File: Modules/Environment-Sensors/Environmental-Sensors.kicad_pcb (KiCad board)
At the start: 2 copper layers, 20.3 x 18.4 mm, 15 parts, among them J1 Conn_01x04, U1 CCS811, U2 ENS210, U3 BMP280

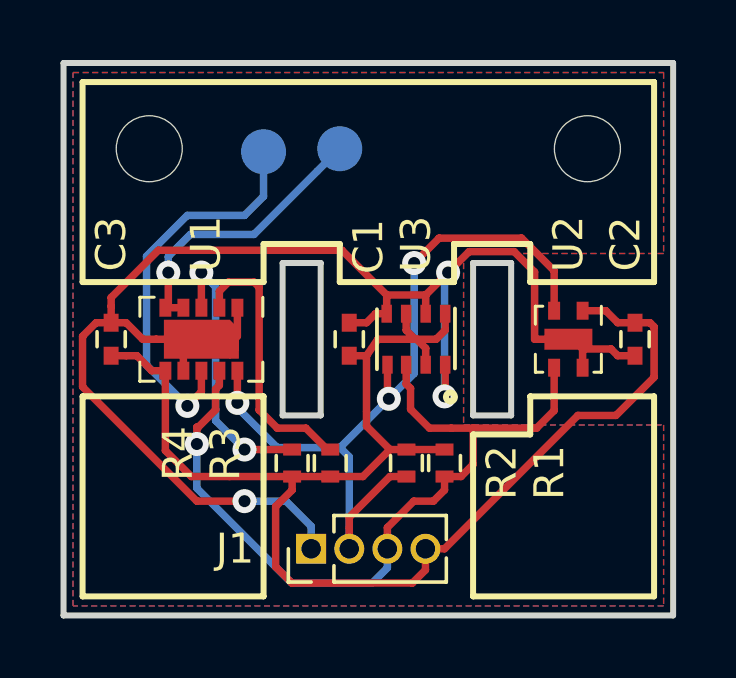
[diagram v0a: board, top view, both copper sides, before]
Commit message: Added board v1.1.0 of environmental sensors
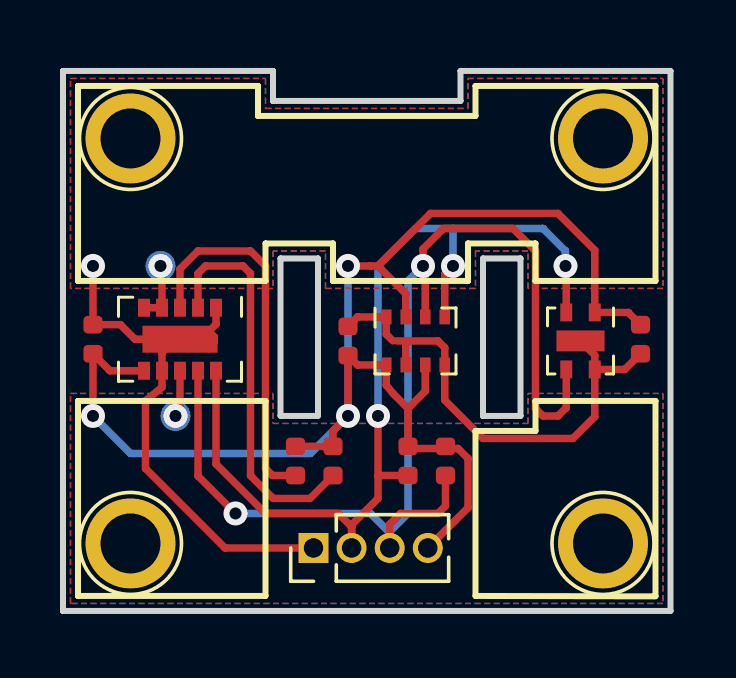
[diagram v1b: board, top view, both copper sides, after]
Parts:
- added MK3: Mounting_Hole, TestPoint:TestPoint_Plated_Hole_D2.0mm, F.Cu at (126.2, 86.5)
- added MK4: Mounting_Hole, TestPoint:TestPoint_Plated_Hole_D2.0mm, F.Cu at (110.5, 86.5)
- C1, C2, C3: footprint Capacitors_SMD:C_0402 -> Capacitor_SMD:C_0402_1005Metric
- J1: footprint Pin_Headers:Pin_Header_Straight_1x04_Pitch1.27mm -> Connector_PinHeader_1.27mm:PinHeader_1x04_P1.27mm_Vertical
- MK1, MK2: footprint Mounting_Holes:MountingHole_2.2mm_M2_ISO7380 -> TestPoint:TestPoint_Plated_Hole_D2.0mm
- R1, R2, R3, R4: footprint Resistors_SMD:R_0402 -> Resistor_SMD:R_0402_1005Metric
- TP1, TP2: footprint Measurement_Points:Measurement_Point_Round-SMD-Pad_Small -> TestPoint:TestPoint_Pad_D1.0mm
- U1: footprint Housings_LGA:AMS_LGA-10-1EP_2.7x4mm_Pitch0.6mm -> Package_LGA:AMS_LGA-10-1EP_2.7x4mm_P0.6mm-2
- U2: footprint Housings_DFN_QFN:AMS_QFN-4-1EP_2x2mm_Pitch0.95mm -> Package_DFN_QFN:AMS_QFN-4-1EP_2x2mm_P0.95mm_EP0.7x1.6mm
- U3: footprint Footprints:BMP280_LGA-8 -> Package_LGA:Bosch_LGA-8_2x2.5mm_P0.65mm_ClockwisePinNumbering
- moved TP1 9.28 mm to (112.0, 82.2)
- moved TP2 7.14 mm to (111.5, 77.2)
- moved MK1 0.71 mm to (110.5, 73.0)
- moved U1 0.71 mm to (112.2, 79.7)
- moved MK2 0.62 mm to (126.2, 73.0)
- moved C3 0.61 mm to (109.2, 79.7)
- moved U2 0.41 mm to (125.5, 79.8)
- moved C2 0.18 mm to (127.5, 79.7)
- moved R4 0.13 mm to (116.0, 83.8), turned to 90 degrees
- moved R3 0.12 mm to (117.2, 83.8), turned to 90 degrees
- moved R2 0.09 mm to (119.8, 83.8)
- moved J1 0.08 mm to (116.6, 86.7)
- moved R1 0.08 mm to (121.0, 83.8)
- moved C1 0.07 mm to (117.8, 79.8)
- moved U3 0.06 mm to (120.0, 79.8), turned to 0 degrees
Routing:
- net GND: track 51.7 -> 36.9 mm, vias 3 -> 1
- net /SDA: track 26.9 -> 40.1 mm, vias 1 -> 2
- net Net-(TP1-Pad1): track 13.1 -> 1.57 mm
- net Net-(TP2-Pad1): track 9.23 -> 2.22 mm
- net /SCL: track 27.7 -> 32.3 mm
- net /RESET: track 9.08 -> 13.2 mm
- net /INT: track 9.39 -> 12.4 mm, vias 2 -> 0
- net +3V3: track 48.5 -> 50.3 mm, vias 0 -> 3
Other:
- board size 20.3 x 18.4 mm -> 20.2 x 18 mm
- net class Default: clearance 0.2 -> 0.11
- rule trace_clearance: 0.2 -> 0.11
- board text added: "BasilFX 08/2018 V1.1.0"
